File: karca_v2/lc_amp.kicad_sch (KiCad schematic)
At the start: 19 parts, among them U18 TS5A3159ADBVR, U19 AD8223, U6 TLV9304xD, U7 TLV9304xD

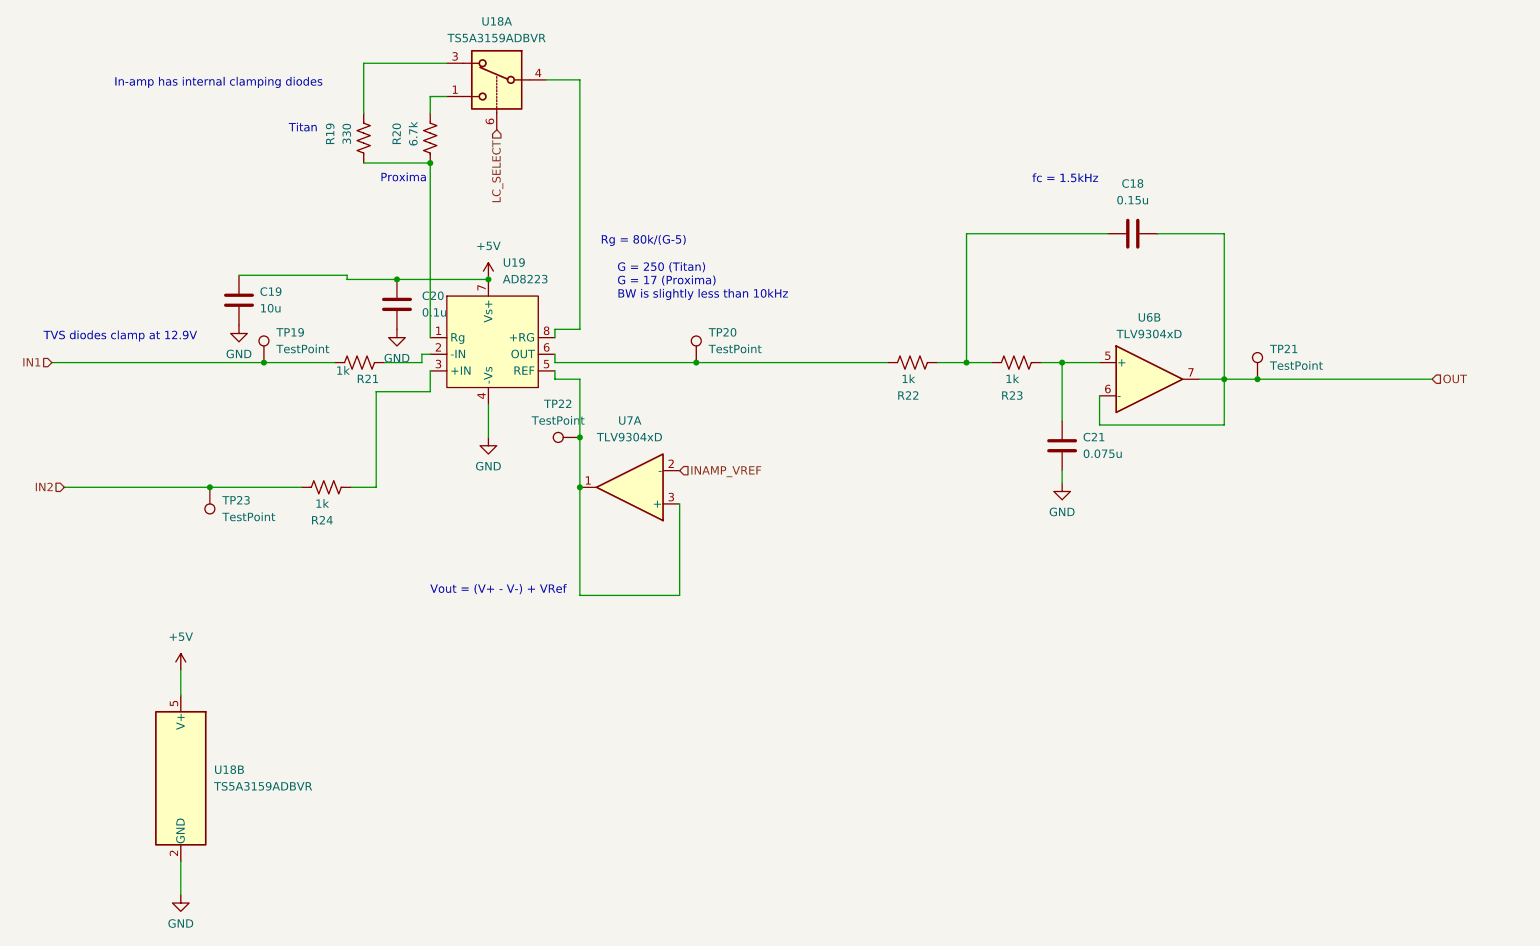
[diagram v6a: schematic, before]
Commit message: replaced digital switches with jumpers, simpler design
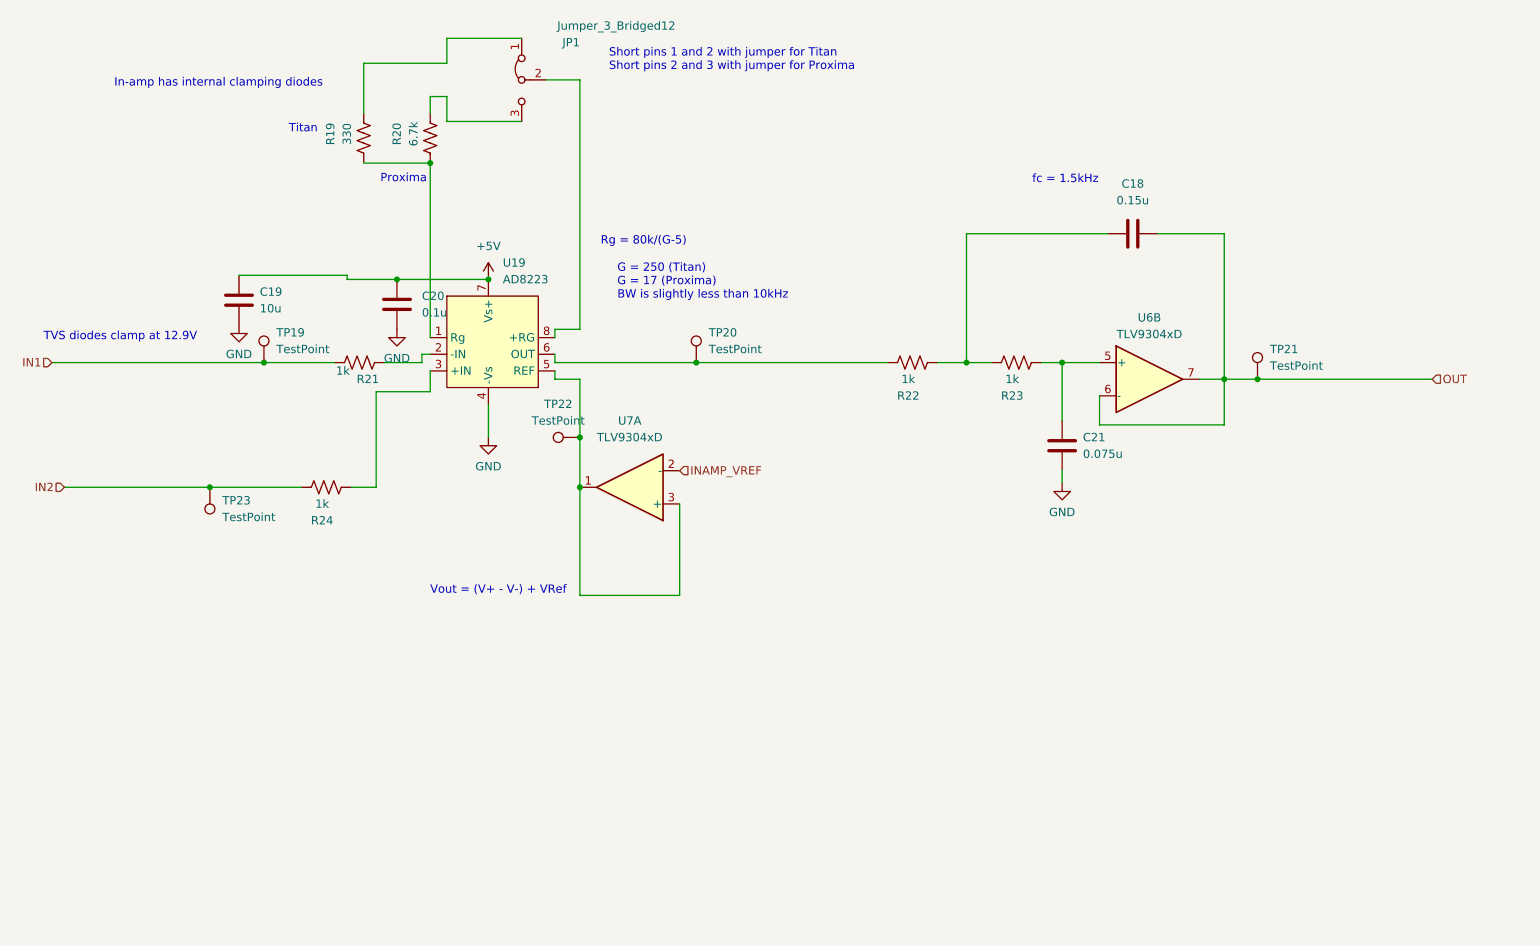
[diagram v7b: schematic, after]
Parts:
- removed U18: TS5A3159ADBVR, Package_TO_SOT_SMD:SOT-23-6, symbol Analog_Switch:TS5A3159ADBVR
- added JP1: Jumper_3_Bridged12, Connector_PinHeader_2.00mm:PinHeader_1x03_P2.00mm_Vertical, symbol Jumper:Jumper_3_Bridged12
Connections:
- net at R20.2: now also JP1.3 (B)
- net at R19.2: now also JP1.1 (A)
- net at U19.8 (+RG): now also JP1.2 (C)
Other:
- note added: "Short pins 1 and 2 with jumper for Titan Short pins 2 and 3 with jumper for Proxima"
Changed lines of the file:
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@@
+    (stroke (width 0) (type default))
+  )
+  (wire (pts (xy 97.79 25.4) (xy 86.36 25.4))
+    (stroke (width 0) (type default))
+  )
+  (wire (pts (xy 86.36 38.1) (xy 86.36 34.29))
     (stroke (width 0) (type default))
   )
@@
     (stroke (width 0) (type default))
   )
-  (wire (pts (xy 45.72 121.92) (xy 45.72 125.73))
+  (wire (pts (xy 86.36 25.4) (xy 86.36 29.21))
     (stroke (width 0) (type default))
   )
@@
     (stroke (width 0) (type default))
   )
+  (wire (pts (xy 97.79 38.1) (xy 86.36 38.1))
+    (stroke (width 0) (type default))
+  )
   (wire (pts (xy 73.66 29.21) (xy 73.66 36.83))
     (stroke (width 0) (type default))
@@
   )
   (wire (pts (xy 78.74 62.23) (xy 92.71 62.23))
-    (stroke (width 0) (type default))
-  )
-  (wire (pts (xy 45.72 151.13) (xy 45.72 156.21))
     (stroke (width 0) (type default))
   )
@@
   )
   (text "Vout = (V+ - V-) + VRef" (at 83.82 110.49 0)
+    (effects (font (size 1.27 1.27)) (justify left bottom))
+  )
+  (text "Short pins 1 and 2 with jumper for Titan\nShort pins 2 and 3 with jumper for Proxima"
+    (at 111.125 30.48 0)
     (effects (font (size 1.27 1.27)) (justify left bottom))
   )
@@
   (hierarchical_label "OUT" (shape input) (at 236.855 77.47 0) (fields_autoplaced)
     (effects (font (size 1.27 1.27)) (justify left))
-  )
-  (hierarchical_label "LC_SELECT" (shape input) (at 93.98 39.37 270) (fields_autoplaced)
-    (effects (font (size 1.27 1.27)) (justify right))
   )
   (symbol (lib_id "Amplifier_Operational:TLV9304xD") (at 114.3 93.98 180) (unit 1)
@@
     )
   )
+  (symbol (lib_id "Jumper:Jumper_3_Bridged12") (at 97.79 31.75 90) (mirror x) (unit 1)
+    (in_bom yes) (on_board yes) (dnp no)
+    (property "Reference" "JP1" (at 106.68 26.035 90)
+      (effects (font (size 1.27 1.27)) (justify left))
+    )
+    (property "Value" "Jumper_3_Bridged12" (at 121.285 23.495 90)
+      (effects (font (size 1.27 1.27)) (justify left))
+    )
+    (property "Footprint" "Connector_PinHeader_2.00mm:PinHeader_1x03_P2.00mm_Vertical" (at 97.79 31.75 0)
+      (effects (font (size 1.27 1.27)) hide)
+    )
+    (property "Datasheet" "~" (at 97.79 31.75 0)
+      (effects (font (size 1.27 1.27)) hide)
+    )
+    (pin "2")
+    (pin "1")
+    (pin "3")
+    (instances
+      (project "karca_v2"
+        (path "/29cf4797-56f2-4f57-ae95-7df639362e3c/ddbef897-b93d-4056-8606-b8e89931524a/592ac910-f9a7-4404-90f3-e507c08d3633"
+          (reference "JP1") (unit 1)
+        )
+        (path "/29cf4797-56f2-4f57-ae95-7df639362e3c/ddbef897-b93d-4056-8606-b8e89931524a/67c0501e-595c-4b66-aaf5-f511fba00546"
+          (reference "JP2") (unit 1)
+        )
+        (path "/29cf4797-56f2-4f57-ae95-7df639362e3c/ddbef897-b93d-4056-8606-b8e89931524a/a97215da-164a-4e9e-8509-0b10a846e98d"
+          (reference "JP3") (unit 1)
+        )
+        (path "/29cf4797-56f2-4f57-ae95-7df639362e3c/ddbef897-b93d-4056-8606-b8e89931524a/bc96a098-6b50-45fa-b7f8-d933c0ccdce6"
+          (reference "JP4") (unit 1)
+        )
+      )
+    )
+  )
   (symbol (lib_id "Device:C") (at 191.135 55.245 270) (unit 1)
     (in_bom yes) (on_board yes) (dnp no) (fields_autoplaced)
@@
     )
   )
-  (symbol (lib_id "power:+5V") (at 45.72 121.92 0) (unit 1)
-    (in_bom yes) (on_board yes) (dnp no) (fields_autoplaced)
-    (property "Reference" "#PWR078" (at 45.72 125.73 0)
-      (effects (font (size 1.27 1.27)) hide)
-    )
-    (property "Value" "+5V" (at 45.72 116.84 0)
-      (effects (font (size 1.27 1.27)))
-    )
-    (property "Footprint" "" (at 45.72 121.92 0)
-      (effects (font (size 1.27 1.27)) hide)
-    )
-    (property "Datasheet" "" (at 45.72 121.92 0)
-      (effects (font (size 1.27 1.27)) hide)
-    )
-    (pin "1")
-    (instances
-      (project "karca_v2"
-        (path "/29cf4797-56f2-4f57-ae95-7df639362e3c/ddbef897-b93d-4056-8606-b8e89931524a/592ac910-f9a7-4404-90f3-e507c08d3633"
-          (reference "#PWR078") (unit 1)
-        )
-        (path "/29cf4797-56f2-4f57-ae95-7df639362e3c/ddbef897-b93d-4056-8606-b8e89931524a/67c0501e-595c-4b66-aaf5-f511fba00546"
-          (reference "#PWR085") (unit 1)
-        )
-        (path "/29cf4797-56f2-4f57-ae95-7df639362e3c/ddbef897-b93d-4056-8606-b8e89931524a/a97215da-164a-4e9e-8509-0b10a846e98d"
-          (reference "#PWR092") (unit 1)
-        )
-        (path "/29cf4797-56f2-4f57-ae95-7df639362e3c/ddbef897-b93d-4056-8606-b8e89931524a/bc96a098-6b50-45fa-b7f8-d933c0ccdce6"
-          (reference "#PWR099") (unit 1)
-        )
-      )
-    )
-  )
-  (symbol (lib_id "Analog_Switch:TS5A3159ADBVR") (at 45.72 138.43 0) (mirror y) (unit 2)
-    (in_bom yes) (on_board yes) (dnp no) (fields_autoplaced)
-    (property "Reference" "U18" (at 50.8 137.16 0)
-      (effects (font (size 1.27 1.27)) (justify right))
-    )
-    (property "Value" "TS5A3159ADBVR" (at 50.8 139.7 0)
-      (effects (font (size 1.27 1.27)) (justify right))
-    )
-    (property "Footprint" "Package_TO_SOT_SMD:SOT-23-6" (at 45.085 151.765 0)
-      (effects (font (size 1.27 1.27)) (justify left) hide)
-    )
-    (property "Datasheet" "http://www.ti.com/lit/ds/symlink/ts5a3159a.pdf" (at 45.085 149.86 0)
-      (effects (font (size 1.27 1.27)) (justify left) hide)
-    )
-    (pin "5")
-    (pin "2")
-    (pin "1")
-    (pin "6")
-    (pin "4")
-    (pin "3")
-    (instances
-      (project "karca_v2"
-        (path "/29cf4797-56f2-4f57-ae95-7df639362e3c/ddbef897-b93d-4056-8606-b8e89931524a/592ac910-f9a7-4404-90f3-e507c08d3633"
-          (reference "U18") (unit 2)
-        )
-        (path "/29cf4797-56f2-4f57-ae95-7df639362e3c/ddbef897-b93d-4056-8606-b8e89931524a/67c0501e-595c-4b66-aaf5-f511fba00546"
-          (reference "U20") (unit 2)
-        )
-        (path "/29cf4797-56f2-4f57-ae95-7df639362e3c/ddbef897-b93d-4056-8606-b8e89931524a/a97215da-164a-4e9e-8509-0b10a846e98d"
-          (reference "U22") (unit 2)
-        )
-        (path "/29cf4797-56f2-4f57-ae95-7df639362e3c/ddbef897-b93d-4056-8606-b8e89931524a/bc96a098-6b50-45fa-b7f8-d933c0ccdce6"
-          (reference "U24") (unit 2)
-        )
-      )
-    )
-  )
   (symbol (lib_id "power:+5V") (at 92.71 62.23 0) (unit 1)
     (in_bom yes) (on_board yes) (dnp no) (fields_autoplaced)
@@
         (path "/29cf4797-56f2-4f57-ae95-7df639362e3c/ddbef897-b93d-4056-8606-b8e89931524a/bc96a098-6b50-45fa-b7f8-d933c0ccdce6"
           (reference "TP35") (unit 1)
-        )
-      )
-    )
-  )
-  (symbol (lib_id "Analog_Switch:TS5A3159ADBVR") (at 93.98 31.75 0) (mirror y) (unit 1)
-    (in_bom yes) (on_board yes) (dnp no) (fields_autoplaced)
-    (property "Reference" "U18" (at 93.98 22.86 0)
-      (effects (font (size 1.27 1.27)))
-    )
-    (property "Value" "TS5A3159ADBVR" (at 93.98 25.4 0)
-      (effects (font (size 1.27 1.27)))
-    )
-    (property "Footprint" "Package_TO_SOT_SMD:SOT-23-6" (at 93.345 45.085 0)
-      (effects (font (size 1.27 1.27)) (justify left) hide)
-    )
-    (property "Datasheet" "http://www.ti.com/lit/ds/symlink/ts5a3159a.pdf" (at 93.345 43.18 0)
-      (effects (font (size 1.27 1.27)) (justify left) hide)
-    )
-    (pin "5")
-    (pin "2")
-    (pin "1")
-    (pin "6")
-    (pin "4")
-    (pin "3")
-    (instances
-      (project "karca_v2"
-        (path "/29cf4797-56f2-4f57-ae95-7df639362e3c/ddbef897-b93d-4056-8606-b8e89931524a/592ac910-f9a7-4404-90f3-e507c08d3633"
-          (reference "U18") (unit 1)
-        )
-        (path "/29cf4797-56f2-4f57-ae95-7df639362e3c/ddbef897-b93d-4056-8606-b8e89931524a/67c0501e-595c-4b66-aaf5-f511fba00546"
-          (reference "U20") (unit 1)
-        )
-        (path "/29cf4797-56f2-4f57-ae95-7df639362e3c/ddbef897-b93d-4056-8606-b8e89931524a/a97215da-164a-4e9e-8509-0b10a846e98d"
-          (reference "U22") (unit 1)
-        )
-        (path "/29cf4797-56f2-4f57-ae95-7df639362e3c/ddbef897-b93d-4056-8606-b8e89931524a/bc96a098-6b50-45fa-b7f8-d933c0ccdce6"
-          (reference "U24") (unit 1)
         )
       )
@@
         )
       )
-    )
-  )
-  (symbol (lib_id "power:GND") (at 45.72 156.21 0) (unit 1)
-    (in_bom yes) (on_board yes) (dnp no) (fields_autoplaced)
-    (property "Reference" "#PWR079" (at 45.72 162.56 0)
-      (effects (font (size 1.27 1.27)) hide)
-    )
-    (property "Value" "GND" (at 45.72 160.655 0)
-      (effects (font (size 1.27 1.27)))
-    )
-    (property "Footprint" "" (at 45.72 156.21 0)
-      (effects (font (size 1.27 1.27)) hide)
-    )
-    (property "Datasheet" "" (at 45.72 156.21 0)
-      (effects (font (size 1.27 1.27)) hide)
-    )
-    (pin "1")
-    (instances
-      (project "karca_v2"
-        (path "/29cf4797-56f2-4f57-ae95-7df639362e3c/ddbef897-b93d-4056-8606-b8e89931524a/592ac910-f9a7-4404-90f3-e507c08d3633"
-          (reference "#PWR079") (unit 1)
-        )
-        (path "/29cf4797-56f2-4f57-ae95-7df639362e3c/ddbef897-b93d-4056-8606-b8e89931524a/67c0501e-595c-4b66-aaf5-f511fba00546"
-          (reference "#PWR086") (unit 1)
-        )
-        (path "/29cf4797-56f2-4f57-ae95-7df639362e3c/ddbef897-b93d-4056-8606-b8e89931524a/a97215da-164a-4e9e-8509-0b10a846e98d"
-          (reference "#PWR093") (unit 1)
-        )
-        (path "/29cf4797-56f2-4f57-ae95-7df639362e3c/ddbef897-b93d-4056-8606-b8e89931524a/bc96a098-6b50-45fa-b7f8-d933c0ccdce6"
-          (reference "#PWR0100") (unit 1)
-        )
-      )

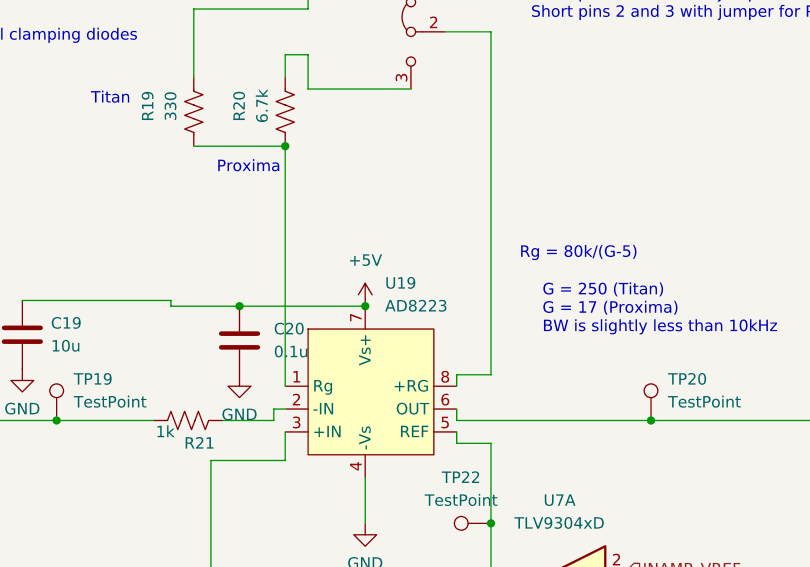
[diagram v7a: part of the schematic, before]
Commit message: Passed all DRC, Added safety jumper to isolate regulators from rest of the board
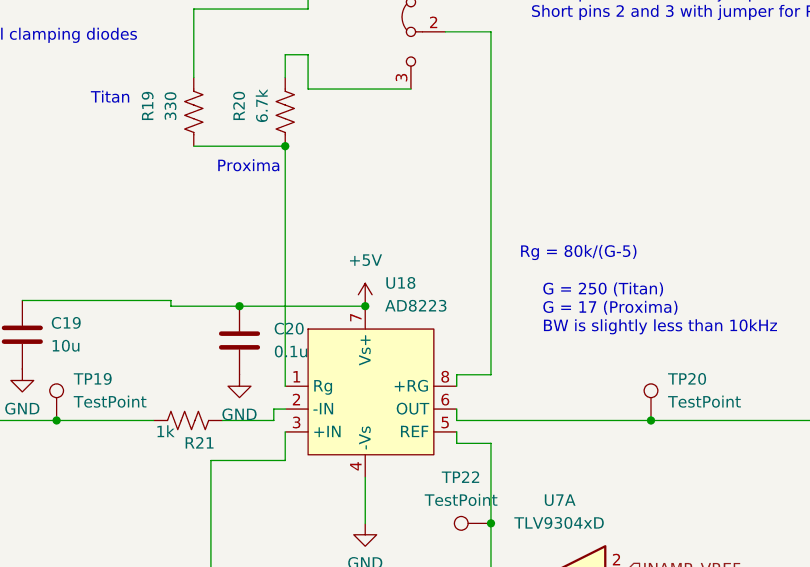
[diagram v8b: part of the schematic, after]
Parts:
- renumbered U19 to U18
